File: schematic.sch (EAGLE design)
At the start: 21 parts, among them IC1 TPS6300, J1 FTDI_DEVICE, U1 ATMEGA328P_TQFP, U2 GY-521MPU6050

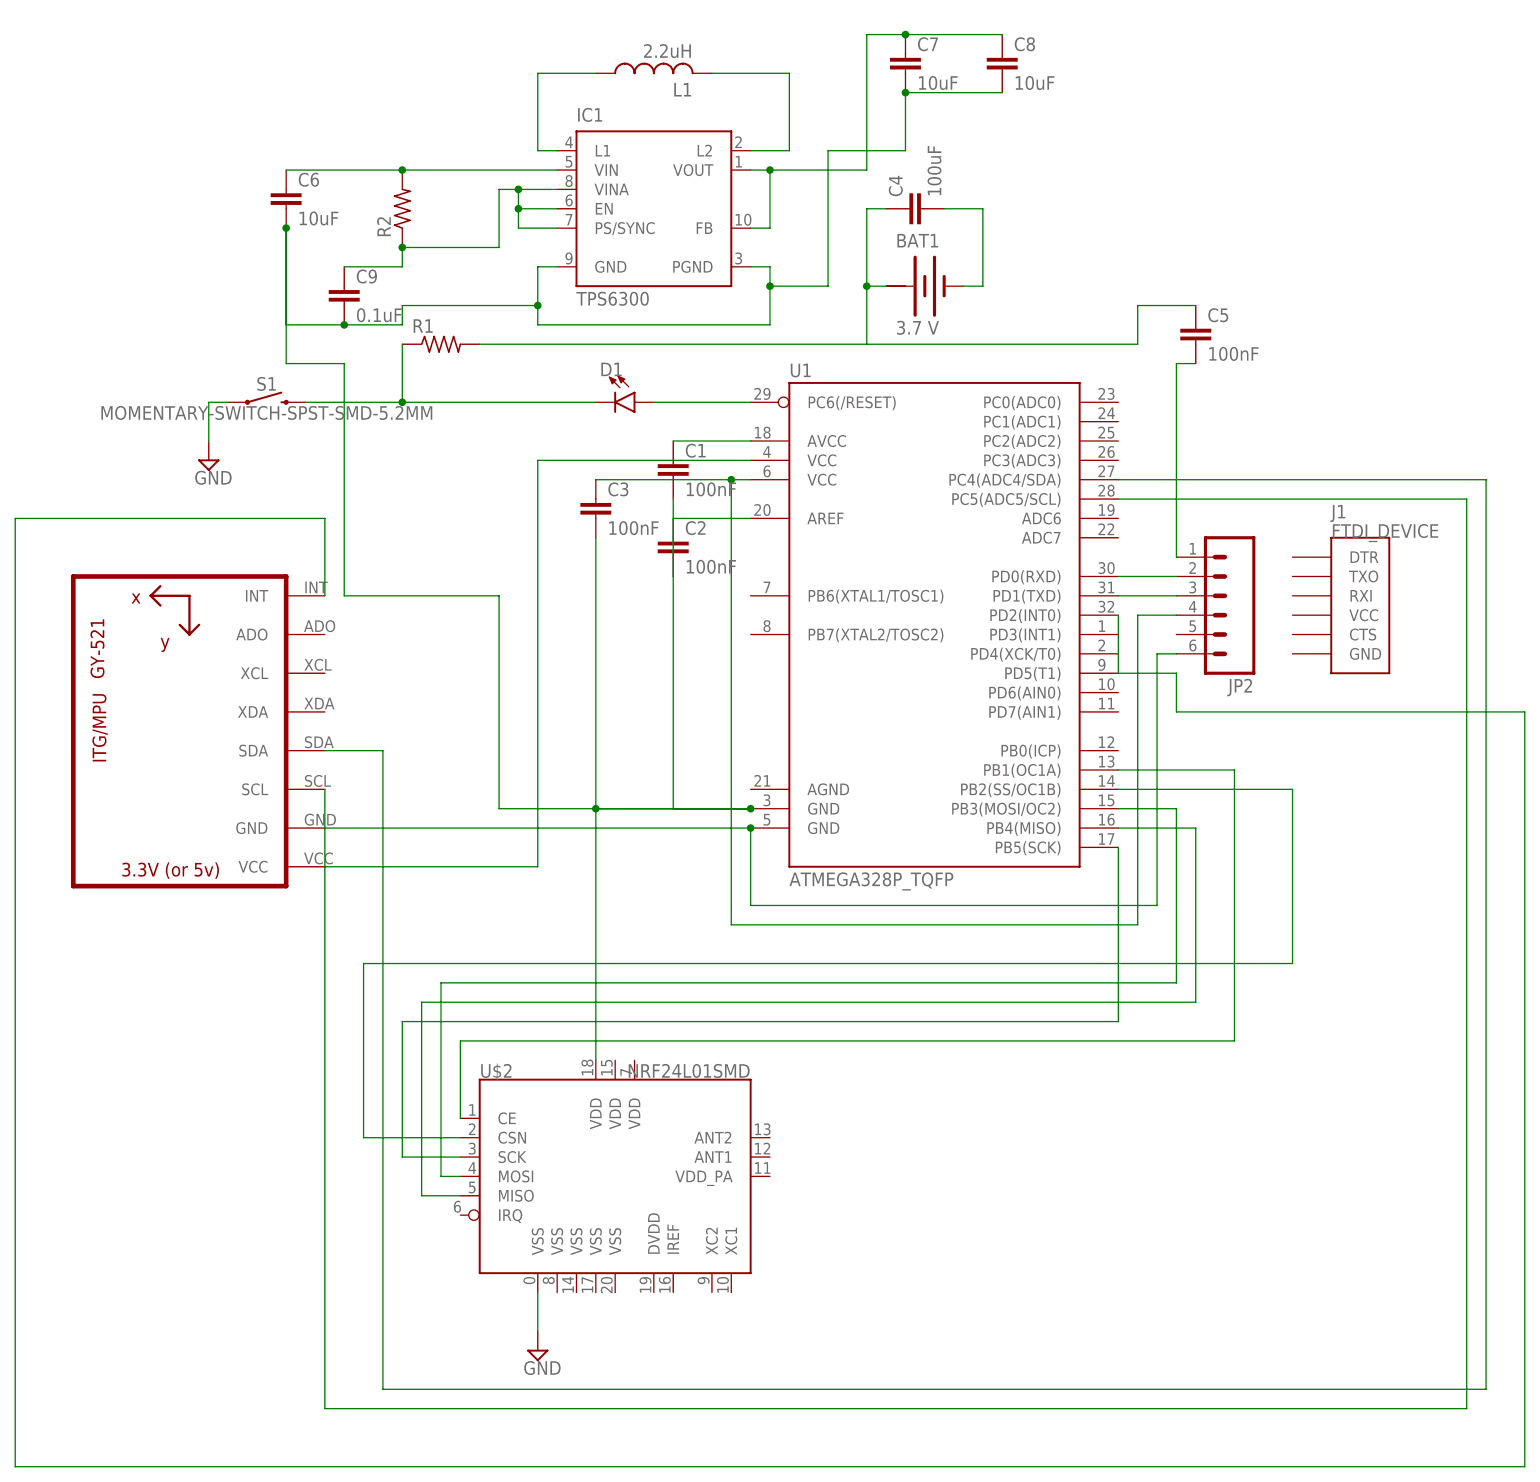
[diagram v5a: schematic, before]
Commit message: Added JST connector
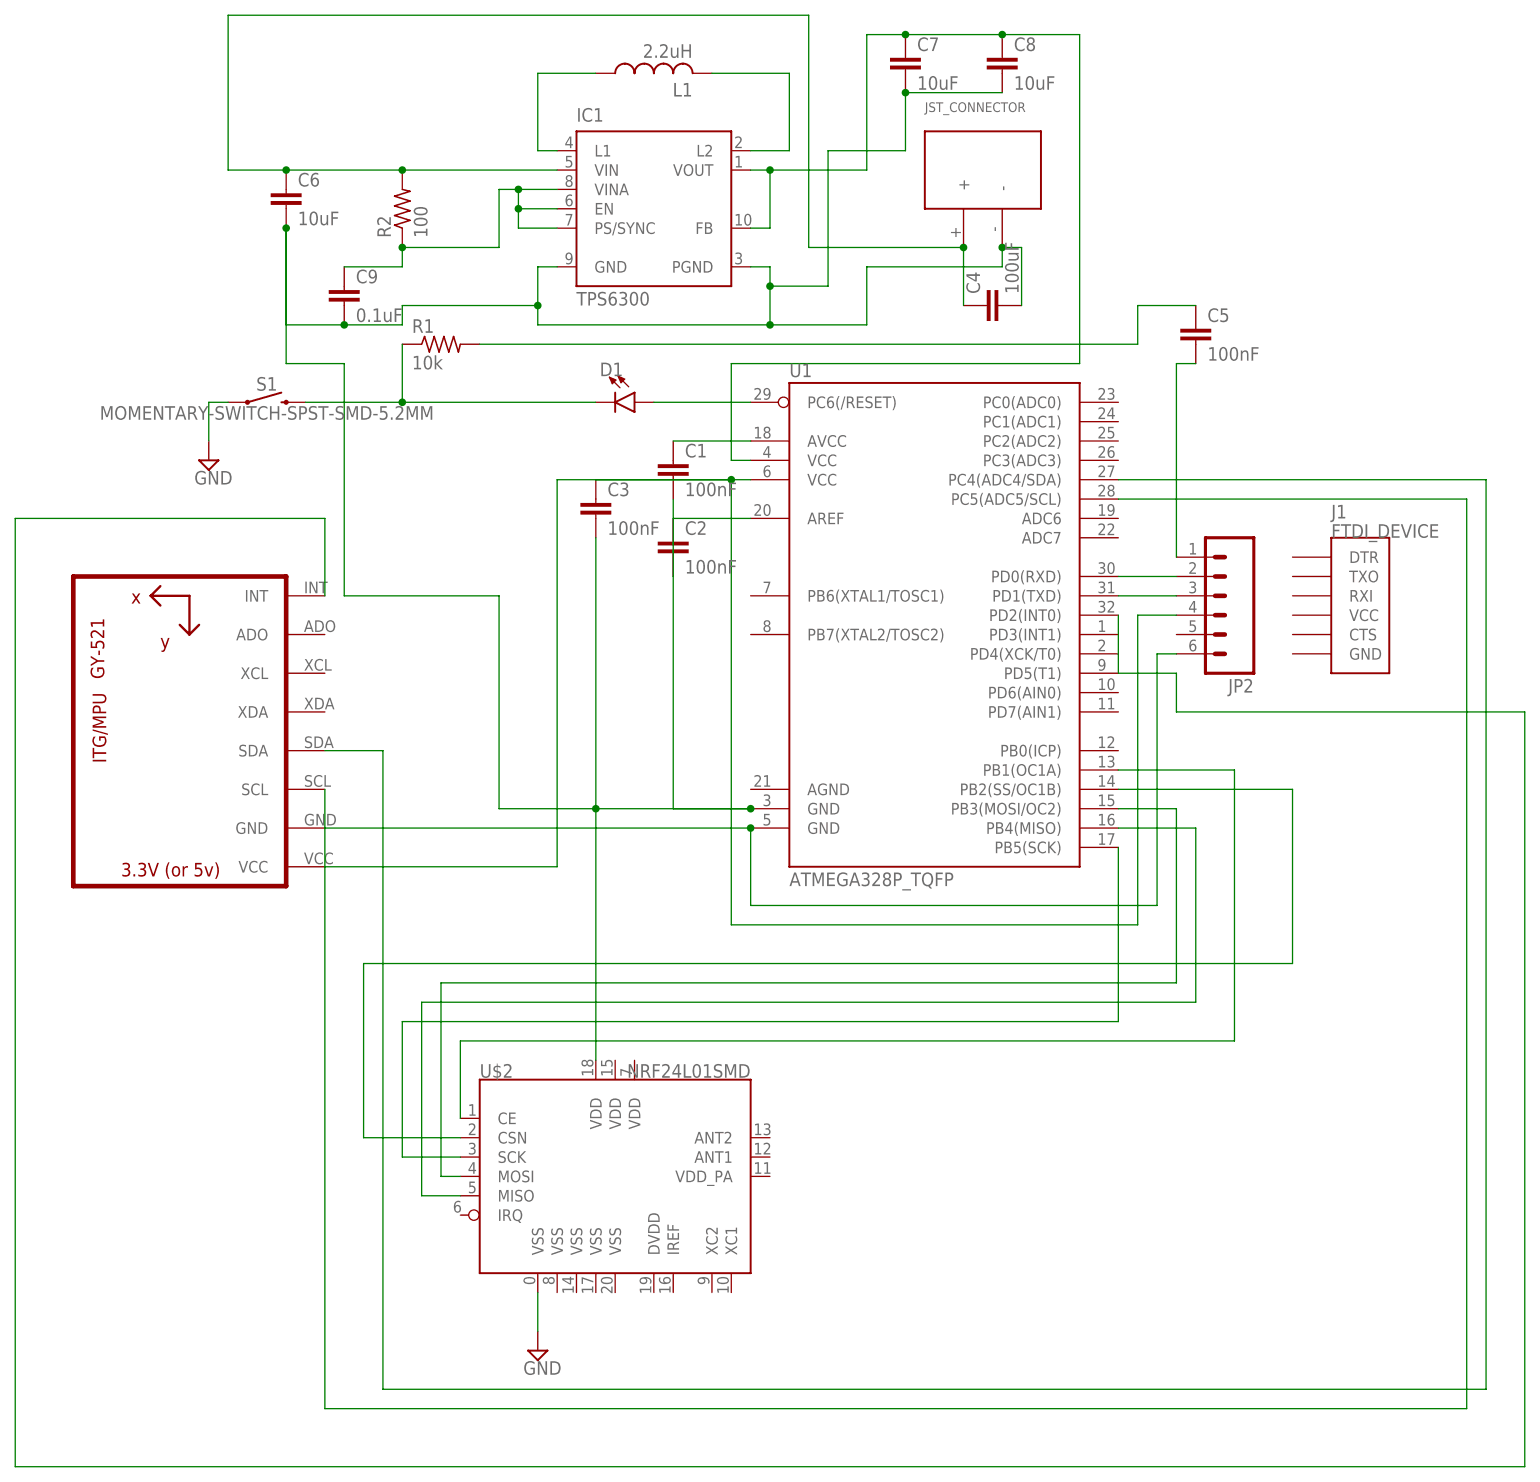
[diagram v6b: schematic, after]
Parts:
- removed BAT1: 3.7 V, special:BATTERY
- added U$1: JST_CONNECTOR_FEMALE, quad:JST_CONNECTOR_FEMALE
- R1: value (none) -> 10k
- R2: value (none) -> 100
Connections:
- removed net N$27: C6.1, IC1G$1.VIN, R2.2
- removed net N$29: C1.2, C2.2, C3.2, C6.2, C7.2, C8.2, C9.2, IC1G$1.GND, IC1G$1.PGND, U$2.VDD@18, U1.GND@3
- removed net N$5: C3.1, JP2.4, U1.VCC@6
- removed net N$8: BAT1.+, C4.1
- new net N$6: C4.1, C6.1, IC1G$1.VIN, R2.2, U$1.+
- net N$16: now also C3.1, JP2.4, U1.VCC@6; no longer U1.VCC@4
- net N$25: now also U1.VCC@4
- net N$7: now also C1.2, C2.2, C3.2, C6.2, C7.2, C8.2, C9.2, IC1G$1.GND, IC1G$1.PGND, U$1.-, U$2.VDD@18, U1.GND@3; no longer BAT1.-
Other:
- moved on the sheet: C4
